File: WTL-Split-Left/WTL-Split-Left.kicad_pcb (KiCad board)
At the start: 2 copper layers, 142.9 x 77.8 mm, 48 parts, among them J1 MJ-4PP-9, U1 ProMicro

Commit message: 1.0 version
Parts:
- added REF**: ToolingHole, kicadPepe:ToolingHole, F.Cu at (200.8, 29.4)
- added REF**: ToolingHole, kicadPepe:ToolingHole, F.Cu at (215.1, 99.2)
- added REF**: ToolingHole, kicadPepe:ToolingHole, F.Cu at (75.4, 43.7)
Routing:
- net GND: track 183.5 -> 3.26 mm
- net col8: track 173.2 -> 176.5 mm
- added copper zone on B.Cu, net (none)
- added copper zone on F.Cu, net (none)
- added copper zone on B.Cu, net GND
- added copper zone on F.Cu, net GND
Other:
- board text added: "Willing To Live SplitL"
- board text added: "desing by sat1l"

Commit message: I don't remember what i've done
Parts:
- MX14, MX22: footprint MX_Only:MXOnly-2U-NoLED -> MX_Only:MXOnly-2U-ReversedStabilizers-NoLED
- moved D13 17.5 mm to (187.3, 46.8)
- moved D19 17.5 mm to (196.8, 65.9)
- moved D23 17.5 mm to (196.8, 84.9)
- moved D6 12.0 mm to (196.5, 37.6), turned to 45 degrees
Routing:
- net GND: track 3.26 -> 184.4 mm
- net row1: track 153.4 -> 222.9 mm, vias 1 -> 0
- net row4: track 127.3 -> 107.1 mm
- net row3: track 111.0 -> 93.7 mm
- net row2: track 104.8 -> 88.0 mm
- net Net-(D19-Pad2): track 3.35 -> 14.8 mm
- net Net-(D23-Pad2): track 3.35 -> 14.8 mm
- net Net-(D13-Pad2): track 3.35 -> 14.8 mm
- net Net-(D6-Pad2): track 3.35 -> 9.89 mm
- net +5V: track 151.9 -> 157.7 mm
- removed copper zone on B.Cu, net (none)
- removed copper zone on F.Cu, net (none)
- removed copper zone on B.Cu, net GND
- removed copper zone on F.Cu, net GND
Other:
- net class Default removed

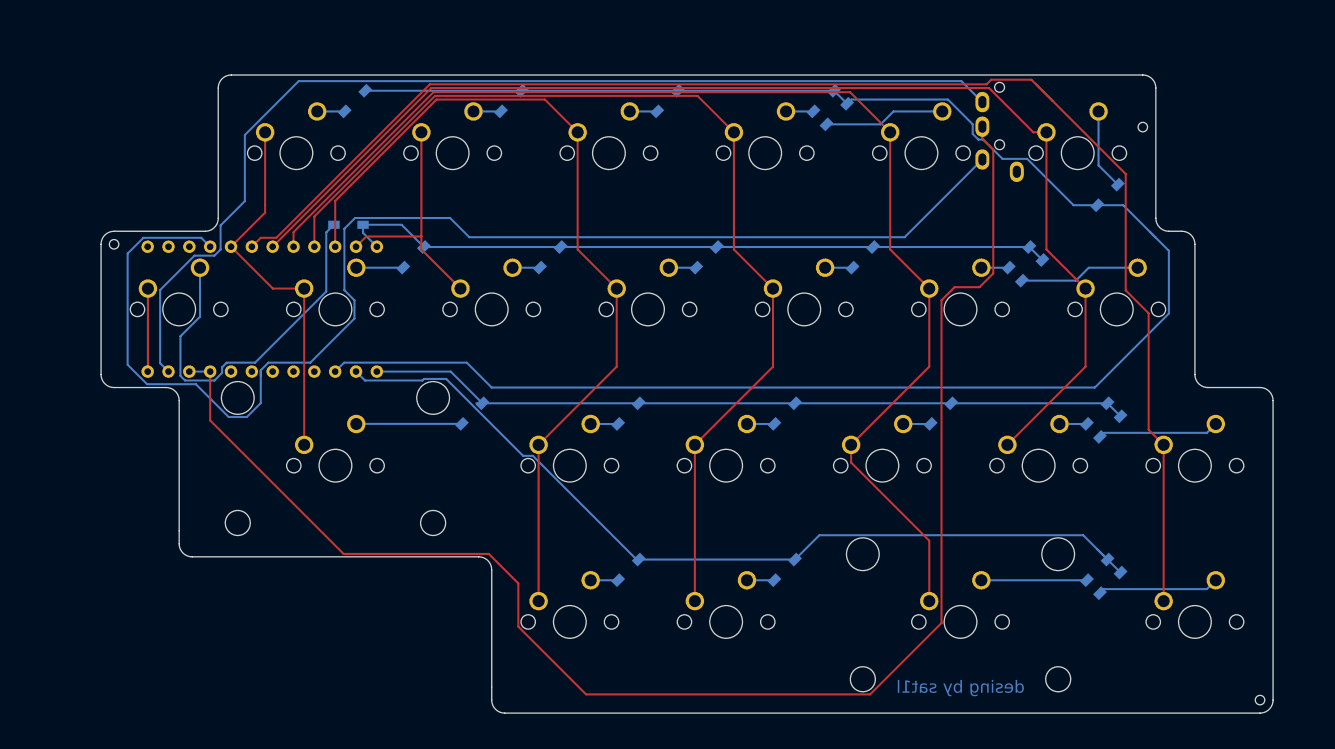
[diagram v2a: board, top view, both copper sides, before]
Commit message: changes shift key on left half from 2u to 2.25u
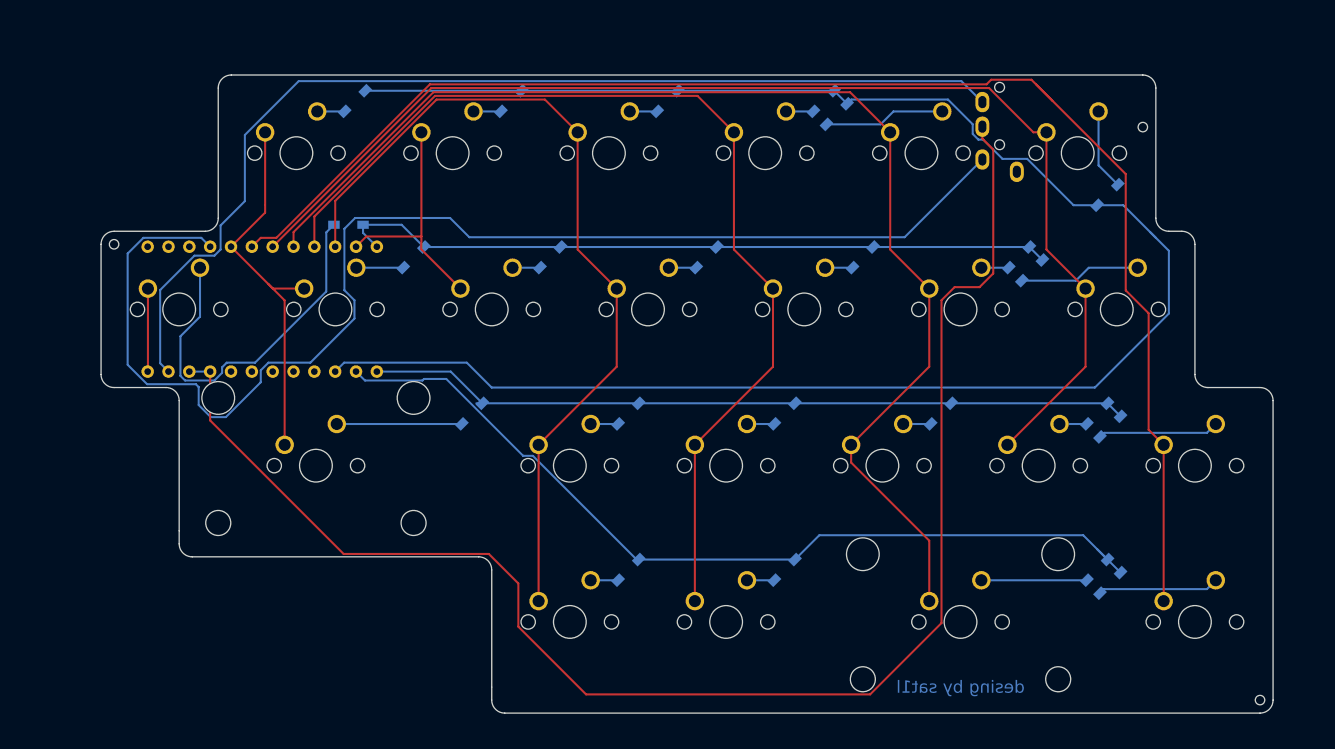
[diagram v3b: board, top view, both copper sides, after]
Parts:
- MX14: footprint MX_Only:MXOnly-2U-ReversedStabilizers-NoLED -> MX_Only:MXOnly-2.25U-ReversedStabilizers-NoLED
- moved MX14 2.38 mm to (100.0, 70.6)
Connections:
- J1 pad A: Net-(J1-PadA) -> unconnected-(J1-PadA)
- U1 pad 22: Net-(U1-Pad22) -> unconnected-(U1-Pad22)
- U1 pad 23: Net-(U1-Pad23) -> unconnected-(U1-Pad23)
- U1 pad 24: Net-(U1-Pad24) -> unconnected-(U1-Pad24)
- U1 pad 5: Net-(U1-Pad5) -> unconnected-(U1-Pad5)
- U1 pad 6: Net-(U1-Pad6) -> unconnected-(U1-Pad6)
- U1 pad 7: Net-(U1-Pad7) -> unconnected-(U1-Pad7)
- U1 pad 8: Net-(U1-Pad8) -> unconnected-(U1-Pad8)
- U1 pad 9: Net-(U1-Pad9) -> unconnected-(U1-Pad9)
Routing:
- net Net-(D14-Pad2): track 12.9 -> 15.3 mm
- net col2: track 45.8 -> 47.2 mm
- net +5V: track 157.7 -> 156.9 mm

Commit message: tf i did?
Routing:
- net col8: track 176.5 -> 173.7 mm
- net row4: track 107.1 -> 106.0 mm
- net row1: track 222.9 -> 221.9 mm
- net col2: track 47.2 -> 46.4 mm
- net row3: track 93.7 -> 92.9 mm
- net GND: track 184.4 -> 183.6 mm
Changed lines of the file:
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@@
   (segment (start 121.44375 61.11875) (end 194.974752 61.11875) (width 0.25) (layer "B.Cu") (net 2))
   (segment (start 192.375248 38.89375) (end 195.2625 38.89375) (width 0.25) (layer "B.Cu") (net 2))
-  (segment (start 202.40625 42.8625) (end 201.719751 42.176001) (width 0.25) (layer "B.Cu") (net 2))
+  (segment (start 198.4375 38.89375) (end 203.99375 44.45) (width 0.25) (layer "B.Cu") (net 2))
   (segment (start 181.362258 30.89376) (end 183.712238 33.24374) (width 0.25) (layer "B.Cu") (net 2))
-  (segment (start 203.99375 44.45) (end 198.4375 38.89375) (width 0.25) (layer "B.Cu") (net 2))
   (segment (start 183.712238 33.24374) (end 186.725238 33.24374) (width 0.25) (layer "B.Cu") (net 2))
   (segment (start 163.180115 24.938635) (end 164.767615 26.526135) (width 0.25) (layer "B.Cu") (net 2))
@@
   (segment (start 102.5525 65.56375) (end 117.7925 65.56375) (width 0.25) (layer "B.Cu") (net 16))
   (segment (start 196.517615 63.038635) (end 198.105115 64.626135) (width 0.25) (layer "B.Cu") (net 17))
-  (segment (start 120.317615 63.038635) (end 119.566386 63.038635) (width 0.25) (layer "B.Cu") (net 17))
   (segment (start 120.317615 63.038635) (end 116.45238 59.1734) (width 0.25) (layer "B.Cu") (net 17))
   (segment (start 116.45238 59.1734) (end 107.442 59.1734) (width 0.25) (layer "B.Cu") (net 17))
@@
   (segment (start 125.273145 69.443749) (end 126.464751 69.443749) (width 0.25) (layer "B.Cu") (net 24))
   (segment (start 104.902 59.1734) (end 105.989001 60.260401) (width 0.25) (layer "B.Cu") (net 24))
-  (segment (start 196.12074 81.69176) (end 196.517615 82.088635) (width 0.25) (layer "B.Cu") (net 24))
+  (segment (start 193.548829 79.119849) (end 196.517615 82.088635) (width 0.25) (layer "B.Cu") (net 24))
   (segment (start 158.417615 82.088635) (end 161.386401 79.119849) (width 0.25) (layer "B.Cu") (net 24))
   (segment (start 113.186927 60.069849) (end 115.899245 60.069849) (width 0.25) (layer "B.Cu") (net 24))
@@
   (segment (start 112.996375 60.260401) (end 113.186927 60.069849) (width 0.25) (layer "B.Cu") (net 24))
   (segment (start 126.464751 69.443749) (end 139.109637 82.088635) (width 0.25) (layer "B.Cu") (net 24))
-  (segment (start 193.548829 79.119849) (end 196.12074 81.69176) (width 0.25) (layer "B.Cu") (net 24))
-  (segment (start 195.288729 80.859749) (end 196.12074 81.69176) (width 0.25) (layer "B.Cu") (net 24))
   (segment (start 161.386401 79.119849) (end 193.548829 79.119849) (width 0.25) (layer "B.Cu") (net 24))
   (segment (start 115.899245 60.069849) (end 125.273145 69.443749) (width 0.25) (layer "B.Cu") (net 24))
@@
   (segment (start 178.702597 23.765097) (end 181.25625 26.31875) (width 0.25) (layer "B.Cu") (net 30))
   (segment (start 88.392212 44.29195) (end 88.392212 41.35519) (width 0.25) (layer "B.Cu") (net 30))
-  (segment (start 94.1943 48.4857) (end 94.76235 49.05375) (width 0.25) (layer "F.Cu") (net 31))
   (segment (start 93.82125 39.79415) (end 89.662 43.9534) (width 0.25) (layer "F.Cu") (net 31))
   (segment (start 96.2025 68.10375) (end 96.195489 68.096739) (width 0.25) (layer "F.Cu") (net 31))
   (segment (start 96.195489 68.096739) (end 96.195489 50.486889) (width 0.25) (layer "F.Cu") (net 31))
-  (segment (start 93.82125 38.883888) (end 93.82125 39.79415) (width 0.25) (layer "F.Cu") (net 31))
-  (segment (start 89.662 43.9534) (end 94.1943 48.4857) (width 0.25) (layer "F.Cu") (net 31))
-  (segment (start 96.195489 50.486889) (end 94.1943 48.4857) (width 0.25) (layer "F.Cu") (net 31))
+  (segment (start 93.82125 30.00375) (end 93.82125 39.79415) (width 0.25) (layer "F.Cu") (net 31))
+  (segment (start 89.662 43.9534) (end 96.195489 50.486889) (width 0.25) (layer "F.Cu") (net 31))
   (segment (start 94.76235 49.05375) (end 98.58375 49.05375) (width 0.25) (layer "F.Cu") (net 31))
-  (segment (start 93.82125 30.00375) (end 93.82125 38.883888) (width 0.25) (layer "F.Cu") (net 31))
   (segment (start 112.87125 30.00375) (end 112.87125 42.70375) (width 0.25) (layer "F.Cu") (net 32))
   (segment (start 104.902 43.9534) (end 106.15165 42.70375) (width 0.25) (layer "F.Cu") (net 32))
@@
   (segment (start 95.192591 42.866399) (end 113.90275 24.15624) (width 0.25) (layer "F.Cu") (net 38))
   (segment (start 198.733749 35.092251) (end 198.733749 49.274849) (width 0.25) (layer "F.Cu") (net 38))
-  (segment (start 187.797738 24.15624) (end 189.770749 26.129251) (width 0.25) (layer "F.Cu") (net 38))
+  (segment (start 187.235247 23.593749) (end 198.733749 35.092251) (width 0.25) (layer "F.Cu") (net 38))
   (segment (start 182.331241 23.593749) (end 187.235247 23.593749) (width 0.25) (layer "F.Cu") (net 38))
   (segment (start 201.523749 52.064849) (end 201.523749 66.268749) (width 0.25) (layer "F.Cu") (net 38))
@@
   (segment (start 201.523749 66.268749) (end 203.35875 68.10375) (width 0.25) (layer "F.Cu") (net 38))
   (segment (start 181.76875 24.15624) (end 182.331241 23.593749) (width 0.25) (layer "F.Cu") (net 38))
-  (segment (start 187.235247 23.593749) (end 189.770749 26.129251) (width 0.25) (layer "F.Cu") (net 38))
-  (segment (start 189.770749 26.129251) (end 198.733749 35.092251) (width 0.25) (layer "F.Cu") (net 38))
   (segment (start 103.390238 81.40624) (end 121.09374 81.40624) (width 0.25) (layer "F.Cu") (net 47))
   (segment (start 180.912651 48.880851) (end 182.583751 47.209751) (width 0.25) (layer "F.Cu") (net 47))
@@
   (segment (start 124.688749 85.001249) (end 124.688749 90.269751) (width 0.25) (layer "F.Cu") (net 47))
   (segment (start 181.25625 30.787752) (end 181.25625 29.31875) (width 0.25) (layer "F.Cu") (net 47))
-  (segment (start 181.76875 29.83125) (end 181.25625 29.31875) (width 0.25) (layer "F.Cu") (net 47))
   (segment (start 87.122 59.1734) (end 87.122 65.138002) (width 0.25) (layer "F.Cu") (net 47))
   (segment (start 176.274849 50.480677) (end 177.874675 48.880851) (width 0.25) (layer "F.Cu") (net 47))
